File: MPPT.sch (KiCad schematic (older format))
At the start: 124 parts, among them J1 Solar Array, J2 Battery, J3 Car Power, J4 CAN_In, J5 CAN_Out, Q1 NMOS, Q2 NMOS, SW1 RESET, SW2 CAN Address, U1 PQMC3-D12-S9-S, U2 Nucleo_L432KC, U3 UCC37321, U4 INA210, U5 ADM3055E, U6 INA210, U7 CDSOT23-T24CAN, U8 MAX400_option2, U9 MAX400_option2

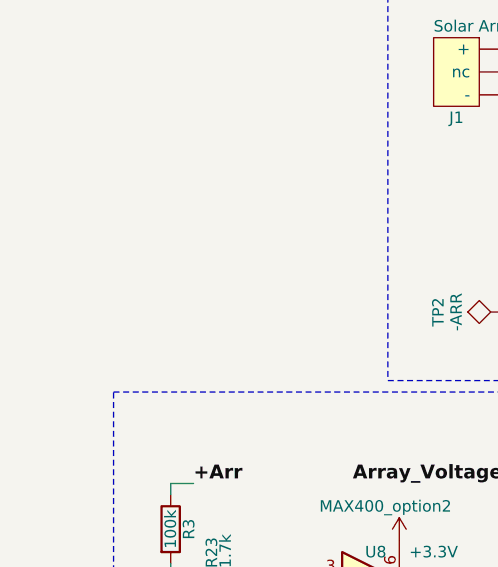
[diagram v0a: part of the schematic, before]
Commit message: added back in heatsinks and generated gerber.
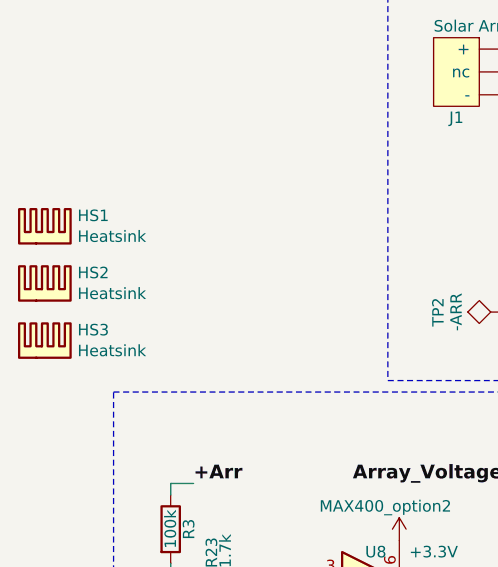
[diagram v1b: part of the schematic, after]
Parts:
- added HS1, HS2, HS3: Heatsink, Heatsink:Heatsink_Fischer_SK129-STS_42x25mm_2xDrill2.5mm, symbol Mechanical:Heatsink
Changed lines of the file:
@@
+	1    0    0    -1
+$EndComp
+$Comp
+L Mechanical:Heatsink HS2
+U 1 1 5F5B266C
+P -950 2300
+F 0 "HS2" H -808 2421 50  0000 L CNN
+F 1 "Heatsink" H -808 2330 50  0000 L CNN
+F 2 "Heatsink:Heatsink_Fischer_SK129-STS_42x25mm_2xDrill2.5mm" H -938 2300 50  0001 C CNN
+F 3 "~" H -938 2300 50  0001 C CNN
+	1    -950 2300
+	1    0    0    -1
+$EndComp
+$Comp
+L Mechanical:Heatsink HS3
+U 1 1 5F5B5FD7
+P -950 2550
+F 0 "HS3" H -808 2671 50  0000 L CNN
+F 1 "Heatsink" H -808 2580 50  0000 L CNN
+F 2 "Heatsink:Heatsink_Fischer_SK129-STS_42x25mm_2xDrill2.5mm" H -938 2550 50  0001 C CNN
+F 3 "~" H -938 2550 50  0001 C CNN
+	1    -950 2550
+	1    0    0    -1
+$EndComp
+$Comp
+L Mechanical:Heatsink HS1
+U 1 1 5F5B6CE9
+P -950 2050
+F 0 "HS1" H -808 2171 50  0000 L CNN
+F 1 "Heatsink" H -808 2080 50  0000 L CNN
+F 2 "Heatsink:Heatsink_Fischer_SK129-STS_42x25mm_2xDrill2.5mm" H -938 2050 50  0001 C CNN
+F 3 "~" H -938 2050 50  0001 C CNN
+	1    -950 2050
 	1    0    0    -1
 $EndComp

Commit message: Major MPPT Board update. Overhaul of layout, and cleanup of the schematic. Added further documentation and updated instructions in the README. Added unity gain op amp for voltage sensors.
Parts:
- removed LED4: Battery Full?, LEDs:LED_0805_HandSoldering, symbol MPPT-rescue:LED_ALT
- removed R15: 330R, Resistors_SMD:R_0805_HandSoldering, symbol MPPT-rescue:R_Small
- removed SW2: CAN Address, Buttons_Switches_THT:SW_DIP_x4_W7.62mm_Slide_LowProfile, symbol MPPT-rescue:SW_DIP_x04
- added F1: Fuse, MPPT-PrimaryPCB:05200101Z_Fuze_Holder_5x20_PCB_Mount, symbol Device:Fuse
- added H1: Top Left Mounting Hole, MountingHole:MountingHole_3.2mm_M3, symbol Mechanical:MountingHole
- added H2: Top Right Mounting Hole, MountingHole:MountingHole_3.2mm_M3, symbol Mechanical:MountingHole
- added H3: Bottom Left Mounting Hole, MountingHole:MountingHole_3.2mm_M3, symbol Mechanical:MountingHole
- added H4: Bottom Right Mounting Hole, MountingHole:MountingHole_3.2mm_M3, symbol Mechanical:MountingHole
- added LED10: BPS Full (Blue), LED_SMD:LED_0805_2012Metric, symbol Device:LED_ALT
- added LED5: Error (Amber), LED_SMD:LED_0805_2012Metric, symbol Device:LED_ALT
- added R11, R6: 330, Resistor_SMD:R_0805_2012Metric, symbol Device:R_Small
- added SW2: SW_DIP_x02, MPPT-PrimaryPCB:ADF02ST04_DIP_Switch_2_POS, symbol Switch:SW_DIP_x02
- C1: renamed from C6; value 0.1u -> 0.1uF; footprint Capacitors_SMD:C_0805_HandSoldering -> Capacitor_SMD:C_0805_2012Metric; symbol MPPT-rescue:C_Small -> Device:C_Small
- C10: renamed from C2; footprint UTSVT_Passive:CP_Radial_D31mm_P9mm -> Capacitor_THT:CP_Radial_D30.0mm_P10.00mm_SnapIn; symbol MPPT-rescue:CP1 -> Device:CP1
- C11: renamed from C17; footprint Capacitors_SMD:C_0805_HandSoldering -> Capacitor_SMD:C_0805_2012Metric; symbol MPPT-rescue:C_Small -> Device:C_Small
- C12: renamed from C21; footprint Capacitors_SMD:C_0805_HandSoldering -> Capacitor_SMD:C_0805_2012Metric; symbol MPPT-rescue:C_Small -> Device:C_Small
- C13: renamed from C18; footprint Capacitors_SMD:C_0805_HandSoldering -> Capacitor_SMD:C_0805_2012Metric; symbol MPPT-rescue:C_Small -> Device:C_Small
- C14: renamed from C22; footprint Capacitors_SMD:C_0805_HandSoldering -> Capacitor_SMD:C_0805_2012Metric; symbol MPPT-rescue:C_Small -> Device:C_Small
- C15: renamed from C19; footprint Capacitors_SMD:C_0805_HandSoldering -> Capacitor_SMD:C_0805_2012Metric; symbol MPPT-rescue:C_Small -> Device:C_Small
- C16: renamed from C20; footprint Capacitors_SMD:C_0805_HandSoldering -> Capacitor_SMD:C_0805_2012Metric; symbol MPPT-rescue:C_Small -> Device:C_Small
- C17: renamed from C13; value 10u -> 10uF; footprint Capacitors_SMD:C_0805 -> Capacitor_SMD:C_0805_2012Metric; symbol MPPT-rescue:C_Small -> Device:C_Small
- C18: renamed from C14; value 0.1u -> 0.1uF; footprint Capacitors_SMD:C_0805 -> Capacitor_SMD:C_0805_2012Metric; symbol MPPT-rescue:C_Small -> Device:C_Small
- C19: renamed from C15; value 0.1u -> 0.1uF; footprint Capacitors_SMD:C_0805 -> Capacitor_SMD:C_0805_2012Metric; symbol MPPT-rescue:C_Small -> Device:C_Small
- C2: renamed from C7; value 1u -> 1uF; footprint Capacitors_THT:CP_Radial_D10.0mm_P5.00mm -> Capacitor_THT:CP_Radial_D10.0mm_P5.00mm; symbol MPPT-rescue:C_Small -> Device:C_Small
- C20: renamed from C16; value 0.01u -> 0.01uF; footprint Capacitors_SMD:C_0805 -> Capacitor_SMD:C_0805_2012Metric; symbol MPPT-rescue:C_Small -> Device:C_Small
- C21: renamed from C10; value 0.22u -> 0.22uF; footprint Capacitors_SMD:C_0805_HandSoldering -> Capacitor_SMD:C_0805_2012Metric; symbol MPPT-rescue:C_Small -> Device:C_Small
- C22: renamed from C9; value 10u -> 10uF; footprint Capacitors_SMD:C_0805_HandSoldering -> Capacitor_SMD:C_0805_2012Metric; symbol MPPT-rescue:C_Small -> Device:C_Small
- C23: renamed from C12; value 0.01u -> 0.01uF; footprint Capacitors_SMD:C_0805_HandSoldering -> Capacitor_SMD:C_0805_2012Metric; symbol MPPT-rescue:C_Small -> Device:C_Small
- C24: renamed from C11; value 0.1u -> 0.1uF; footprint Capacitors_SMD:C_0805_HandSoldering -> Capacitor_SMD:C_0805_2012Metric; symbol MPPT-rescue:C_Small -> Device:C_Small
- C3: renamed from C8; value 0.1u -> 0.1uF; footprint Capacitors_SMD:C_0805_HandSoldering -> Capacitor_SMD:C_0805_2012Metric; symbol MPPT-rescue:C_Small -> Device:C_Small
- C4: renamed from C24; value 100u -> 100uF; footprint Capacitors_SMD:CP_Elec_6.3x7.7 -> Capacitor_SMD:C_1210_3225Metric; symbol MPPT-rescue:CP1_Small -> Device:CP1_Small
- C5: renamed from C4; value 47u -> 47uF; footprint Capacitors_SMD:CP_Elec_6.3x5.3 -> Capacitor_SMD:C_1210_3225Metric; symbol MPPT-rescue:CP1_Small -> Device:CP1_Small
- C6: renamed from C23; value 10u -> 10uF; footprint Capacitors_SMD:C_0805_HandSoldering -> Capacitor_SMD:C_0805_2012Metric; symbol MPPT-rescue:C_Small -> Device:C_Small
- C7: renamed from C5; value 100u -> 100uF; footprint Capacitors_SMD:CP_Elec_6.3x7.7 -> Capacitor_SMD:C_1210_3225Metric; symbol MPPT-rescue:CP1_Small -> Device:CP1_Small
- C8: renamed from C1; footprint UTSVT_Passive:CP_Radial_D31mm_P9mm -> Capacitor_THT:CP_Radial_D30.0mm_P10.00mm_SnapIn; symbol MPPT-rescue:CP1 -> Device:CP1
- C9: renamed from C3; footprint MPPT_Custom:C_Rect_L26.5mm_W17.0mm_P22.50mm_MKS4 -> (none); symbol MPPT-rescue:CP1 -> Device:CP1
- D1: renamed from D9; value 4V Zener -> 3.9V Zener; footprint Diodes_SMD:D_SOD-123F -> Diode_SMD:D_SOD-123F; symbol MPPT-rescue:D_Zener_Small_ALT -> Device:D_Zener_Small_ALT
- D10: renamed from D14; footprint Diodes_SMD:D_SOD-123 -> Diode_SMD:D_SOD-123F; symbol MPPT-rescue:D_ALT -> Device:D_ALT
- D11: renamed from D5; value 4V Zener -> 3.9V Zener; footprint Diodes_SMD:D_SOD-123F -> Diode_SMD:D_SOD-123F; symbol MPPT-rescue:D_Zener_ALT -> Device:D_Zener_ALT
- D12: renamed from D6; footprint Diodes_SMD:D_SOD-123 -> Diode_SMD:D_SOD-123F; symbol MPPT-rescue:D_ALT -> Device:D_ALT
- D13: renamed from D7; value 4V Zener -> 3.9V Zener; footprint Diodes_SMD:D_SOD-123F -> Diode_SMD:D_SOD-123F; symbol MPPT-rescue:D_Zener_ALT -> Device:D_Zener_ALT
- D14: renamed from D8; footprint Diodes_SMD:D_SOD-123 -> Diode_SMD:D_SOD-123F; symbol MPPT-rescue:D_ALT -> Device:D_ALT
- D2: renamed from D10; footprint Diodes_SMD:D_SOD-123 -> Diode_SMD:D_SOD-123F; symbol MPPT-rescue:D_Small_ALT -> Device:D_Small_ALT
- D3: renamed from D4; value 18V Zener -> 16.3V Zener; footprint Diodes_SMD:D_SMA_Handsoldering -> Diode_SMD:D_SOD-123F; symbol MPPT-rescue:D_Zener_ALT -> Device:D_Zener_ALT
- D4: renamed from D1; footprint TO_SOT_Packages_THT:TO-220-2_Vertical -> Package_TO_SOT_THT:TO-220-2_Vertical; symbol MPPT-rescue:D_Schottky -> Device:D_Schottky
- D5: renamed from D2; footprint TO_SOT_Packages_THT:TO-220-2_Vertical -> Package_TO_SOT_THT:TO-220-2_Vertical; symbol MPPT-rescue:D_Schottky -> Device:D_Schottky
- D6: renamed from D3; footprint TO_SOT_Packages_THT:TO-220-2_Vertical -> Package_TO_SOT_THT:TO-220-2_Vertical; symbol MPPT-rescue:D_Schottky -> Device:D_Schottky
- D7: renamed from D11; value 4V Zener -> 3.9V Zener; footprint Diodes_SMD:D_SOD-123F -> Diode_SMD:D_SOD-123F; symbol MPPT-rescue:D_Zener_ALT -> Device:D_Zener_ALT
- D8: renamed from D12; footprint Diodes_SMD:D_SOD-123 -> Diode_SMD:D_SOD-123F; symbol MPPT-rescue:D_ALT -> Device:D_ALT
- D9: renamed from D13; value 4V Zener -> 3.9V Zener; footprint Diodes_SMD:D_SOD-123F -> Diode_SMD:D_SOD-123F; symbol MPPT-rescue:D_Zener_ALT -> Device:D_Zener_ALT
- F2: renamed from F1; footprint UTSVT_Passive:LittelFuse_OMNIBLOK_520Series_PCB -> MPPT-PrimaryPCB:05200101Z_Fuze_Holder_5x20_PCB_Mount; symbol MPPT-rescue:Fuse -> Device:Fuse
- HS1: value Heatsink -> Schottky Diode Heatsink
- HS2: value Heatsink -> Snubber Heatsink
- HS3: value Heatsink -> MOSFET Heatsink
- J1: renamed from J3; footprint UTSVT_Connectors:Molex_MicroFit3.0_1x2xP3.00mm_PolarizingPeg_Vertical -> Connector_Molex:Molex_Micro-Fit_3.0_43650-0215_1x02_P3.00mm_Vertical; symbol MPPT-rescue:CarPowerConnector -> Array:PWR_Connector_43650-0215
- J2: renamed from J1; footprint UTSVT_Connectors:PhoenixContact_PowerCombicon5_GF_3x7.62mm -> MPPT-PrimaryPCB:PhoenixContact_PowerCombicon5_GF_2x7.62mm; symbol MPPT-rescue:SolarArrayConnector -> Array:PWR_Connector_1720796
- J3: renamed from J2; footprint UTSVT_Connectors:PhoenixContact_PowerCombicon5_GF_2x7.62mm -> MPPT-PrimaryPCB:PhoenixContact_PowerCombicon5_GF_2x7.62mm; symbol MPPT-rescue:BatteryConnector -> Array:PWR_Connector_1720796
- J4, J5: footprint UTSVT_Connectors:Molex_MicroFit3.0_1x4xP3.00mm_PolarizingPeg_Vertical -> Connector_Molex:Molex_Micro-Fit_3.0_43650-0415_1x04_P3.00mm_Vertical; symbol MPPT-rescue:CANConnector -> Array:CAN_Connector_43650-0427
- JP1: footprint Pin_Headers:Pin_Header_Straight_1x02_Pitch2.54mm -> Connector_PinHeader_2.54mm:PinHeader_1x02_P2.54mm_Vertical; symbol MPPT-rescue:Jumper_NO_Small -> Device:Jumper_NO_Small
- L1: renamed from L4; value 4.7u -> 4.7uH; footprint Inductors_SMD:L_0805_HandSoldering -> Inductor_SMD:L_0805_2012Metric; symbol MPPT-rescue:L_Small -> Device:L_Small
- L2: renamed from L1; footprint Inductors_THT:L_Toroid_Vertical_L46.0mm_W19.1mm_P21.80mm_Bourns_5700 -> MPPT-PrimaryPCB:L_Toroid_Vertical_L46.0mm_W19.1mm_P21.80mm_Bourns_5700; symbol MPPT-rescue:L_Core_Ferrite -> Device:L_Core_Ferrite
- L3: renamed from L2; value 2k -> 1.8kH; footprint Inductors_SMD:L_0805_HandSoldering -> Inductor_SMD:L_0805_2012Metric; symbol MPPT-rescue:Ferrite_Bead_Small -> Device:Ferrite_Bead_Small
- L4: renamed from L3; value 2k -> 1.8kH; footprint Inductors_SMD:L_0805_HandSoldering -> Inductor_SMD:L_0805_2012Metric; symbol MPPT-rescue:Ferrite_Bead_Small -> Device:Ferrite_Bead_Small
- LED1: value Array Live? -> Array Live (Green); footprint LEDs:LED_0805_HandSoldering -> LED_SMD:LED_0805_2012Metric; symbol MPPT-rescue:LED_ALT -> Device:LED_ALT
- LED2: value Battery Live? -> Battery Live (Green); footprint LEDs:LED_0805_HandSoldering -> LED_SMD:LED_0805_2012Metric; symbol MPPT-rescue:LED_ALT -> Device:LED_ALT
- LED3: value Car Power Live? -> Car Power Live (Green); footprint LEDs:LED_0805_HandSoldering -> LED_SMD:LED_0805_2012Metric; symbol MPPT-rescue:LED_ALT -> Device:LED_ALT
- LED4: renamed from LED7; value Iso 9V Live? -> Device 9V Live (Green); footprint LEDs:LED_0805_HandSoldering -> LED_SMD:LED_0805_2012Metric; symbol MPPT-rescue:LED_ALT -> Device:LED_ALT
- LED6: renamed from LED5; value Tracking? -> Tracking (Blue); footprint LEDs:LED_0805_HandSoldering -> LED_SMD:LED_0805_2012Metric; symbol MPPT-rescue:LED_ALT -> Device:LED_ALT
- LED7: renamed from LED6; value PWM -> PWM (Blue); footprint LEDs:LED_0805_HandSoldering -> LED_SMD:LED_0805_2012Metric; symbol MPPT-rescue:LED_ALT -> Device:LED_ALT
- LED8: value CAN_Tx -> CAN_Tx (Blue); footprint LEDs:LED_0805_HandSoldering -> LED_SMD:LED_0805_2012Metric; symbol MPPT-rescue:LED_ALT -> Device:LED_ALT
- LED9: value CAN_Rx -> CAN_Rx (Blue); footprint LEDs:LED_0805_HandSoldering -> LED_SMD:LED_0805_2012Metric; symbol MPPT-rescue:LED_ALT -> Device:LED_ALT
- Q1, Q2: footprint TO_SOT_Packages_THT:TO-247_TO-3P_Vertical -> Package_TO_SOT_THT:TO-247-3_Vertical; symbol MPPT-rescue:Q_NMOS_GDS -> Device:Q_NMOS_GDS
- R1: renamed from R7; value 1R5 -> 1.5; footprint Resistors_SMD:R_1206_HandSoldering -> Resistor_SMD:R_0805_2012Metric; symbol MPPT-rescue:R -> Device:R
- R10: renamed from R22; value 330R -> 330; footprint Resistors_SMD:R_0805_HandSoldering -> Resistor_SMD:R_0805_2012Metric; symbol MPPT-rescue:R_Small -> Device:R_Small
- R12: renamed from R2; footprint Resistors_SMD:R_1206_HandSoldering -> Resistor_SMD:R_0805_2012Metric; symbol MPPT-rescue:R -> Device:R
- R13: renamed from R1; footprint Resistors_THT:R_Axial_Power_L20.0mm_W6.4mm_P22.40mm -> (none); symbol MPPT-rescue:R -> Device:R
- R14: renamed from R8; footprint Resistors_SMD:R_2512_HandSoldering -> Resistor_SMD:R_1210_3225Metric; symbol MPPT-rescue:R_Small -> Device:R_Small
- R15: renamed from R18; footprint Resistors_SMD:R_0805_HandSoldering -> Resistor_SMD:R_0805_2012Metric; symbol MPPT-rescue:R_Small -> Device:R_Small
- R16: renamed from R11; footprint Resistors_SMD:R_2512_HandSoldering -> Resistor_SMD:R_1210_3225Metric; symbol MPPT-rescue:R_Small -> Device:R_Small
- R17: renamed from R19; footprint Resistors_SMD:R_0805_HandSoldering -> Resistor_SMD:R_0805_2012Metric; symbol MPPT-rescue:R_Small -> Device:R_Small
- R18: renamed from R3; footprint Resistors_SMD:R_1206_HandSoldering -> Resistor_SMD:R_0805_2012Metric; symbol MPPT-rescue:R -> Device:R
- R19: renamed from R5; footprint Resistors_SMD:R_1206_HandSoldering -> Resistor_SMD:R_0805_2012Metric; symbol MPPT-rescue:R -> Device:R
- R2: renamed from R12; value 40K -> 15k; footprint Resistors_SMD:R_1206_HandSoldering -> Resistor_SMD:R_1206_3216Metric; symbol MPPT-rescue:R_Small -> Device:R_Small
- R20: renamed from R23; footprint Resistors_SMD:R_0805_HandSoldering -> Resistor_SMD:R_0805_2012Metric; symbol MPPT-rescue:R_Small -> Device:R
- R21: renamed from R4; footprint Resistors_SMD:R_1206_HandSoldering -> Resistor_SMD:R_0805_2012Metric; symbol MPPT-rescue:R -> Device:R
- R22: renamed from R6; footprint Resistors_SMD:R_1206_HandSoldering -> Resistor_SMD:R_0805_2012Metric; symbol MPPT-rescue:R -> Device:R
- R23: renamed from R24; footprint Resistors_SMD:R_0805_HandSoldering -> Resistor_SMD:R_0805_2012Metric; symbol MPPT-rescue:R_Small -> Device:R
- R24: renamed from R25; footprint Resistors_SMD:R_0805_HandSoldering -> Resistor_SMD:R_0805_2012Metric; symbol MPPT-rescue:R -> Device:R
- R25: renamed from R10; footprint Resistors_SMD:R_0805_HandSoldering -> Resistor_SMD:R_0805_2012Metric; symbol MPPT-rescue:R -> Device:R
- R26: renamed from R9; footprint Resistors_SMD:R_0805_HandSoldering -> Resistor_SMD:R_0805_2012Metric; symbol MPPT-rescue:R -> Device:R
- R3: renamed from R13; value 40K -> 27k; footprint Resistors_SMD:R_1206_HandSoldering -> Resistor_SMD:R_1206_3216Metric; symbol MPPT-rescue:R_Small -> Device:R_Small
- R4: renamed from R14; value 2K -> 1.5k; footprint Resistors_SMD:R_0805_HandSoldering -> Resistor_SMD:R_0805_2012Metric; symbol MPPT-rescue:R_Small -> Device:R_Small
- R5: renamed from R20; value 1K -> 1.1k; footprint Resistors_SMD:R_0805_HandSoldering -> Resistor_SMD:R_0805_2012Metric; symbol MPPT-rescue:R_Small -> Device:R_Small
- R7: renamed from R16; value 330R -> 330; footprint Resistors_SMD:R_0805_HandSoldering -> Resistor_SMD:R_0805_2012Metric; symbol MPPT-rescue:R_Small -> Device:R_Small
- R8: renamed from R17; value 330R -> 330; footprint Resistors_SMD:R_0805_HandSoldering -> Resistor_SMD:R_0805_2012Metric; symbol MPPT-rescue:R_Small -> Device:R_Small
- R9: renamed from R21; value 330R -> 330; footprint Resistors_SMD:R_0805_HandSoldering -> Resistor_SMD:R_0805_2012Metric; symbol MPPT-rescue:R_Small -> Device:R_Small
- SW1: footprint Buttons_Switches_THT:SW_PUSH_6mm -> Button_Switch_THT:SW_PUSH_6mm; symbol MPPT-rescue:SW_Push -> Switch:SW_Push
- TP1: renamed from TP26; footprint Measurement_Points:Test_Point_Keystone_5005-5009_Compact -> TestPoint:TestPoint_Keystone_5005-5009_Compact; symbol MPPT-rescue:TEST -> Connector:TestPoint
- TP10: renamed from TP3; footprint Measurement_Points:Test_Point_Keystone_5005-5009_Compact -> TestPoint:TestPoint_Keystone_5005-5009_Compact; symbol MPPT-rescue:TEST -> Connector:TestPoint
- TP11: renamed from TP23; footprint Measurement_Points:Test_Point_Keystone_5005-5009_Compact -> TestPoint:TestPoint_Keystone_5005-5009_Compact; symbol MPPT-rescue:TEST -> Connector:TestPoint
- TP12: renamed from TP2; footprint Measurement_Points:Test_Point_Keystone_5005-5009_Compact -> TestPoint:TestPoint_Keystone_5005-5009_Compact; symbol MPPT-rescue:TEST -> Connector:TestPoint
- TP13: renamed from TP12; footprint Measurement_Points:Test_Point_Keystone_5005-5009_Compact -> TestPoint:TestPoint_Keystone_5005-5009_Compact; symbol MPPT-rescue:TEST -> Connector:TestPoint
- TP14: renamed from TP4; footprint Measurement_Points:Test_Point_Keystone_5005-5009_Compact -> TestPoint:TestPoint_Keystone_5005-5009_Compact; symbol MPPT-rescue:TEST -> Connector:TestPoint
- TP15: renamed from TP25; footprint Measurement_Points:Test_Point_Keystone_5005-5009_Compact -> TestPoint:TestPoint_Keystone_5005-5009_Compact; symbol MPPT-rescue:TEST -> Connector:TestPoint
- TP16: renamed from TP24; footprint Measurement_Points:Test_Point_Keystone_5005-5009_Compact -> TestPoint:TestPoint_Keystone_5005-5009_Compact; symbol MPPT-rescue:TEST -> Connector:TestPoint
- TP17: renamed from TP9; footprint Measurement_Points:Test_Point_Keystone_5005-5009_Compact -> TestPoint:TestPoint_Keystone_5005-5009_Compact; symbol MPPT-rescue:TEST -> Connector:TestPoint
- TP18: renamed from TP10; footprint Measurement_Points:Test_Point_Keystone_5005-5009_Compact -> TestPoint:TestPoint_Keystone_5005-5009_Compact; symbol MPPT-rescue:TEST -> Connector:TestPoint
- TP19: renamed from TP7; footprint Measurement_Points:Test_Point_Keystone_5005-5009_Compact -> TestPoint:TestPoint_Keystone_5005-5009_Compact; symbol MPPT-rescue:TEST -> Connector:TestPoint
- TP2: renamed from TP11; footprint Measurement_Points:Test_Point_Keystone_5005-5009_Compact -> TestPoint:TestPoint_Keystone_5005-5009_Compact; symbol MPPT-rescue:TEST -> Connector:TestPoint
- TP20: renamed from TP8; footprint Measurement_Points:Test_Point_Keystone_5005-5009_Compact -> TestPoint:TestPoint_Keystone_5005-5009_Compact; symbol MPPT-rescue:TEST -> Connector:TestPoint
- TP21: renamed from TP19; footprint Measurement_Points:Test_Point_Keystone_5005-5009_Compact -> TestPoint:TestPoint_Keystone_5005-5009_Compact; symbol MPPT-rescue:TEST -> Connector:TestPoint
- TP22: renamed from TP20; footprint Measurement_Points:Test_Point_Keystone_5005-5009_Compact -> TestPoint:TestPoint_Keystone_5005-5009_Compact; symbol MPPT-rescue:TEST -> Connector:TestPoint
- TP23: renamed from TP13; footprint Measurement_Points:Test_Point_Keystone_5005-5009_Compact -> TestPoint:TestPoint_Keystone_5005-5009_Compact; symbol MPPT-rescue:TEST -> Connector:TestPoint
- TP24: renamed from TP14; footprint Measurement_Points:Test_Point_Keystone_5005-5009_Compact -> TestPoint:TestPoint_Keystone_5005-5009_Compact; symbol MPPT-rescue:TEST -> Connector:TestPoint
- TP25: renamed from TP15; footprint Measurement_Points:Test_Point_Keystone_5005-5009_Compact -> TestPoint:TestPoint_Keystone_5005-5009_Compact; symbol MPPT-rescue:TEST -> Connector:TestPoint
- TP26: renamed from TP16; footprint Measurement_Points:Test_Point_Keystone_5005-5009_Compact -> TestPoint:TestPoint_Keystone_5005-5009_Compact; symbol MPPT-rescue:TEST -> Connector:TestPoint
- TP27: renamed from TP21; footprint Measurement_Points:Test_Point_Keystone_5005-5009_Compact -> TestPoint:TestPoint_Keystone_5005-5009_Compact; symbol MPPT-rescue:TEST -> Connector:TestPoint
- TP28: renamed from TP22; footprint Measurement_Points:Test_Point_Keystone_5005-5009_Compact -> TestPoint:TestPoint_Keystone_5005-5009_Compact; symbol MPPT-rescue:TEST -> Connector:TestPoint
- TP3: renamed from TP27; footprint Measurement_Points:Test_Point_Keystone_5005-5009_Compact -> TestPoint:TestPoint_Keystone_5005-5009_Compact; symbol MPPT-rescue:TEST -> Connector:TestPoint
- TP4: renamed from TP28; footprint Measurement_Points:Test_Point_Keystone_5005-5009_Compact -> TestPoint:TestPoint_Keystone_5005-5009_Compact; symbol MPPT-rescue:TEST -> Connector:TestPoint
- TP5: renamed from TP17; footprint Measurement_Points:Test_Point_Keystone_5005-5009_Compact -> TestPoint:TestPoint_Keystone_5005-5009_Compact; symbol MPPT-rescue:TEST -> Connector:TestPoint
- TP6: renamed from TP18; footprint Measurement_Points:Test_Point_Keystone_5005-5009_Compact -> TestPoint:TestPoint_Keystone_5005-5009_Compact; symbol MPPT-rescue:TEST -> Connector:TestPoint
- TP7: renamed from TP5; footprint Measurement_Points:Test_Point_Keystone_5005-5009_Compact -> TestPoint:TestPoint_Keystone_5005-5009_Compact; symbol MPPT-rescue:TEST -> Connector:TestPoint
- TP8: renamed from TP6; footprint Measurement_Points:Test_Point_Keystone_5005-5009_Compact -> TestPoint:TestPoint_Keystone_5005-5009_Compact; symbol MPPT-rescue:TEST -> Connector:TestPoint
- TP9: renamed from TP1; footprint Measurement_Points:Test_Point_Keystone_5005-5009_Compact -> TestPoint:TestPoint_Keystone_5005-5009_Compact; symbol MPPT-rescue:TEST -> Connector:TestPoint
- U1: renamed from U2; footprint UTSVT_Special:NucleoL432KC -> MPPT-PrimaryPCB:MODULE_NUCLEO-L432KC; symbol MPPT-rescue:Nucleo_L432KC -> Array:MCU_Nucleo_L432KC
- U2: renamed from U3; footprint UTSVT_ICs:SOIC-8_4.00x5.00mm_Pitch1.27mm -> Package_SO:SOIC-8_3.9x4.9mm_P1.27mm; symbol MPPT-rescue:UCC37321 -> Array:UCC37321
- U3: renamed from U1; footprint UTSVT_ICs:CUI_PQMC3-S -> MPPT-PrimaryPCB:490_PQMC3_D12_S12_S; symbol MPPT-rescue:PQMC3-Dx-Sx-S -> Array:PWR_REG_PQMC3-Dx-Sx-S
- U4: footprint UTSVT_ICs:SOIC-6_1.40x2.15mm_Pitch0.65mm -> MPPT-PrimaryPCB:SC70-6; symbol MPPT-rescue:INA21x -> Array:OP_AMP_INA21x
- U5: renamed from U6; footprint UTSVT_ICs:SOIC-6_1.40x2.15mm_Pitch0.65mm -> MPPT-PrimaryPCB:SC70-6; symbol MPPT-rescue:INA21x -> Array:OP_AMP_INA21x
- U6: renamed from U8; value MAX400_option2 -> MAX40075AUT+; footprint MPPT_Custom:SOT95P280X145-6N -> Package_TO_SOT_SMD:SOT-23-6; symbol max400_option2-amplifier_current:MAX400_option2-Amplifier_Current -> Array:MAX400_option2-Amplifier_Current
- U7: renamed from U9; value MAX400_option2 -> MAX40075AUT+; footprint MPPT_Custom:SOT95P280X145-6N -> Package_TO_SOT_SMD:SOT-23-6; symbol max400_option2-amplifier_current:MAX400_option2-Amplifier_Current -> Array:MAX400_option2-Amplifier_Current
- U8: renamed from U5; footprint UTSVT_ICs:SOIC-20W_7.5x15.4mm_Pitch1.27mm -> MPPT-PrimaryPCB:ADM3055EBRIZ; symbol MPPT-rescue:ADM3055E -> Array:CAN_Chip_ADM3055E
- U9: renamed from U7; footprint TO_SOT_Packages_SMD:SOT-23W_Handsoldering -> Package_TO_SOT_SMD:SOT-23; symbol MPPT-rescue:CDSOT23-T24CAN -> Array:CAN_Bus_Protector_CDSOT23-T24CAN
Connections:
- net +Arr: now also F1.2; no longer J2.1 (+)
- net -Arr: now also J2.2 (-); no longer J2.3 (-)
- net Array_Current: now also U1.24 (A5); no longer U1.22 (A3)
- net Array_Voltage: now also U1.25 (A6); no longer U1.24 (A5)
- net Battery_Current: now also U1.22 (A3); no longer U1.21 (A2)
- net GNDPWR: now also SW1.2, LED10.1 (K), LED5.1 (K), SW2.1, SW2.2; no longer SW1.1
- net Reset: now also SW1.1; no longer SW1.2
- net at U1.10 (D7): now also SW2.4
- net at U1.11 (D8): now also SW2.3
- net BPS_Full: now reaches U1.12 (D9)
- net BPS_Full: now also R11.2
- net at C23.1, C24.1, J4.1 (5V)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: now also C22.1; no longer C21.1
- net at C23.2, C24.2, J4.2 (GND)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: now also C22.2; no longer C21.2
- net at L3.2, TP23.1, U8.19 (V_ISO_Out): now also C21.1; no longer C22.1
- net at L4.2, TP26.1, U8.18 (GND_ISO_Out)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: now also C21.2; no longer C22.2
- net Battery_Full renamed Error
- net Error: now also R6.2
- new net: F1.1, J2.1 (+)
- new net: LED10.2 (A), R11.1
- new net: LED5.2 (A), R6.1
- no-connect marks 17 -> 18
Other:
- note added: "Changes from 3.1+:\n\nSchematic:\n- Reannotated all component labels and reverted rescued schematic symbols.\n- Rearranged schematic and cleaned up component positioning.\n- Created Array.lib for array-relevant schematic symbols.\n- Swapped out zener diodes going into the uC from 3.6V to 3.9V.\n- Updated the LEDs and resistors for Xx_live indicators.\n- Added Error indicator LED.\n- Shifted pins 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"
- note added: "Check current board and see their values for R12, C9"
- note added: "For decoupling, we\nadd extra capacitors\nand unlink the power\npins on either side."
- note added: "Note that A7 (PA2) and A2 (PA3) are reserved \nfor STLink UART."
- note added: "USB"
- note added: "Voltage dividers fed \ninto a unity gain op \namp"
- note removed: "Basic voltage\ndividers"
- note removed: "For decoupling, we\nadd extra capacitors\nand unlink the power\npins on either side"
- note removed: "RC filter\noptional"
- note removed: "filter\noptional"
- note removed: "pi filter\noptional"
- moved on the sheet: C1, C10, C11, C12, C13, C14, C15, C16, C17, C18, C19, C2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

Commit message: Finalized board layout.
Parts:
- C2: footprint Capacitor_THT:CP_Radial_D10.0mm_P5.00mm -> Capacitor_SMD:C_0805_2012Metric
- C9: footprint (none) -> Capacitor_THT:C_Rect_L16.5mm_W7.0mm_P15.00mm_MKT; symbol Device:CP1 -> Device:C
- R13: footprint (none) -> Package_TO_SOT_THT:TO-220-2_Vertical
- TP8: value GNDP -> Device GND
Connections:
- net GNDPWR: now also C4.2, C5.2, J1.2 (GND), LED3.1 (K), TP6.1, U3.1 (GND); no longer C1.1, C10.2, C11.2, C12.2, C13.2, C14.2, C15.2, C16.2, C17.2, C18.2, C19.2, C2.2, C20.2, C3.2, C6.1, C7.2, C8.2, C9.2, D1.2 (A), D10.2 (A), D11.2 (A), D12.2 (A), D13.2 (A), D14.2 (A), D2.2 (A), D3.2 (A), D7.2 (A), D8.2 (A), D9.2 (A), LED10.1 (K), LED4.1 (K), LED5.1 (K), LED6.1 (K), LED7.1 (K), LED8.1 (K), LED9.1 (K), Q1.3 (S), Q2.3 (S), R12.2, R14.1, R16.2, R19.2, R22.2, SW1.2, SW2.1, SW2.2, TP1.1, TP15.1, TP3.1, TP4.1, TP8.1, U1.29 (GND), U1.4 (GND), U2.4 (AGND), U2.5 (PGND), U3.7 (0V), U4.1 (REF), U4.2 (V-), U4.4 (+), U5.1 (REF), U5.2 (V-), U5.5 (-), U6.2 (VSS), U7.2 (VSS), U8.1 (GND_In), U8.10 (GND_In), U8.2 (GND_In)
- net GNDREF: now also C1.1, C10.2, C11.2, C12.2, C13.2, C14.2, C15.2, C16.2, C17.2, C18.2, C19.2, C2.2, C20.2, C3.2, C6.1, C7.2, C8.2, C9.2, D1.2 (A), D10.2 (A), D11.2 (A), D12.2 (A), D13.2 (A), D14.2 (A), D2.2 (A), D3.2 (A), D7.2 (A), D8.2 (A), D9.2 (A), LED10.1 (K), LED4.1 (K), LED5.1 (K), LED6.1 (K), LED7.1 (K), LED8.1 (K), LED9.1 (K), Q1.3 (S), Q2.3 (S), R12.2, R14.1, R16.2, R19.2, R22.2, SW1.2, SW2.1, SW2.2, TP1.1, TP15.1, TP3.1, TP4.1, TP8.1, U1.29 (GND), U1.4 (GND), U2.4 (AGND), U2.5 (PGND), U3.7 (0V), U4.1 (REF), U4.2 (V-), U4.4 (+), U5.1 (REF), U5.2 (V-), U5.5 (-), U6.2 (VSS), U7.2 (VSS), U8.1 (GND_In), U8.10 (GND_In), U8.2 (GND_In); no longer C4.2, C5.2, J1.2 (GND), LED3.1 (K), TP6.1, U3.1 (GND)
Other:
- note added: "Isolated Power Regions:\n* Device/Board Power\n - +/-Arr\n - +/-Batt\n - +9VA, +5V, +3.3V\n - GNDREF\n* Car Power\n - +12V\n - GNDPWR"
- note added: "R13, C9 are experimental and are through \nhole components with a range of values."
- note removed: "Check current board and see their values for R12, C9"
- note removed: "Isolated Power Regions:\n* High Power/Nucleo\n - +/-Arr\n - +/-Batt\n - +9A, +5V, +3.3V\n - GNDPWR\n* Low Car Power\n - +12V\n - GNDREF"
- note removed: "Voltage dividers fed \ninto a unity gain op \namp"
- moved on the sheet: TP7, TP8

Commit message: Updated README and some little board positionings.
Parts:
- R14, R16: footprint Resistor_SMD:R_1210_3225Metric -> Resistor_SMD:R_1206_3216Metric
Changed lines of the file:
@@
 F 0 "R16" H 10180 4070 50  0000 L CNN
 F 1 "2m" H 10180 4010 50  0000 L CNN
-F 2 "Resistor_SMD:R_1210_3225Metric" H 10150 4050 50  0001 C CNN
+F 2 "Resistor_SMD:R_1206_3216Metric" H 10150 4050 50  0001 C CNN
 F 3 "" H 10150 4050 50  0001 C CNN
 	1    10150 4050
@@
 F 0 "R14" H 7730 4070 50  0000 L CNN
 F 1 "2m" H 7730 4010 50  0000 L CNN
-F 2 "Resistor_SMD:R_1210_3225Metric" H 7700 4050 50  0001 C CNN
+F 2 "Resistor_SMD:R_1206_3216Metric" H 7700 4050 50  0001 C CNN
 F 3 "" H 7700 4050 50  0001 C CNN
 	1    7700 4050
@@
 Connection ~ 850  850
 $Comp
-L power:GNDREF #PWR?
+L power:GNDREF #PWR0121
 U 1 1 5FDE0FE2
 P 8800 3650
-F 0 "#PWR?" H 8800 3400 50  0001 C CNN
+F 0 "#PWR0121" H 8800 3400 50  0001 C CNN
 F 1 "GNDREF" H 8800 3500 50  0000 C CNN
 F 2 "" H 8800 3650 50  0001 C CNN
@@
 $EndComp
 $Comp
-L power:GNDREF #PWR?
+L power:GNDREF #PWR0122
 U 1 1 5FE1343B
 P 11250 3650
-F 0 "#PWR?" H 11250 3400 50  0001 C CNN
+F 0 "#PWR0122" H 11250 3400 50  0001 C CNN
 F 1 "GNDREF" H 11250 3500 50  0000 C CNN
 F 2 "" H 11250 3650 50  0001 C CNN
